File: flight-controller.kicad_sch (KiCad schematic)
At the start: 73 parts, among them J1 USB_C_Receptacle_USB2.0, Q1 AO3400A, SW1 SW_Push, U1 AT32F435RGT7, U2 BMI270, U3 BMP280, U4 W25N01GVZEIG, U5 AT7456E, U6 TPS54302, U7 TPS54302, U8 TLV75733PDBV, U9 USBLC6-2P6, Y1 27MHz

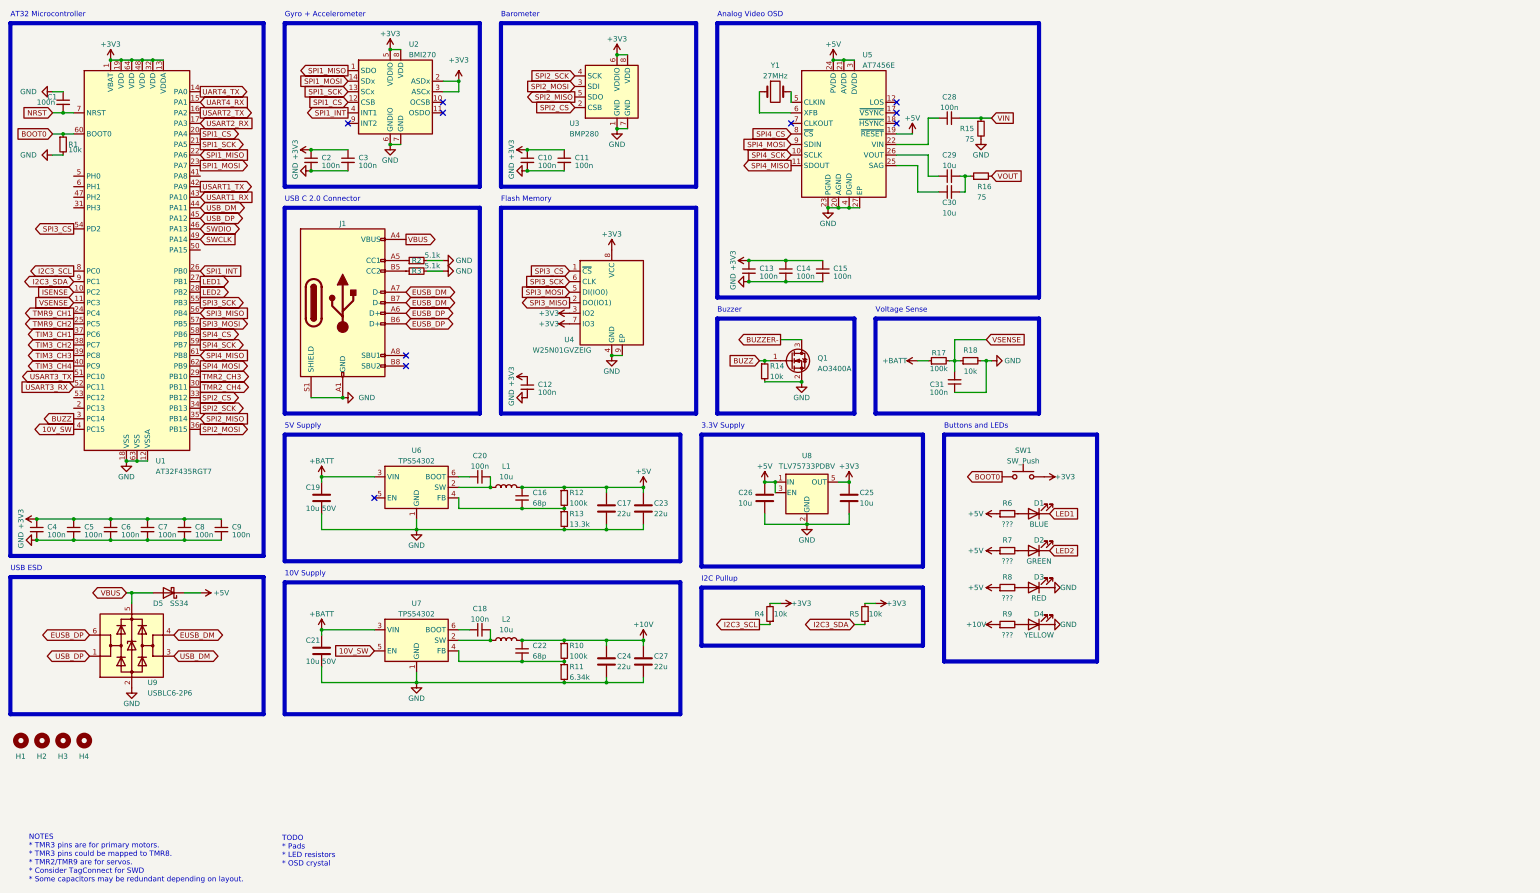
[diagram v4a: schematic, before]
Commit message: Add OSD crystal, minor changes to PCB
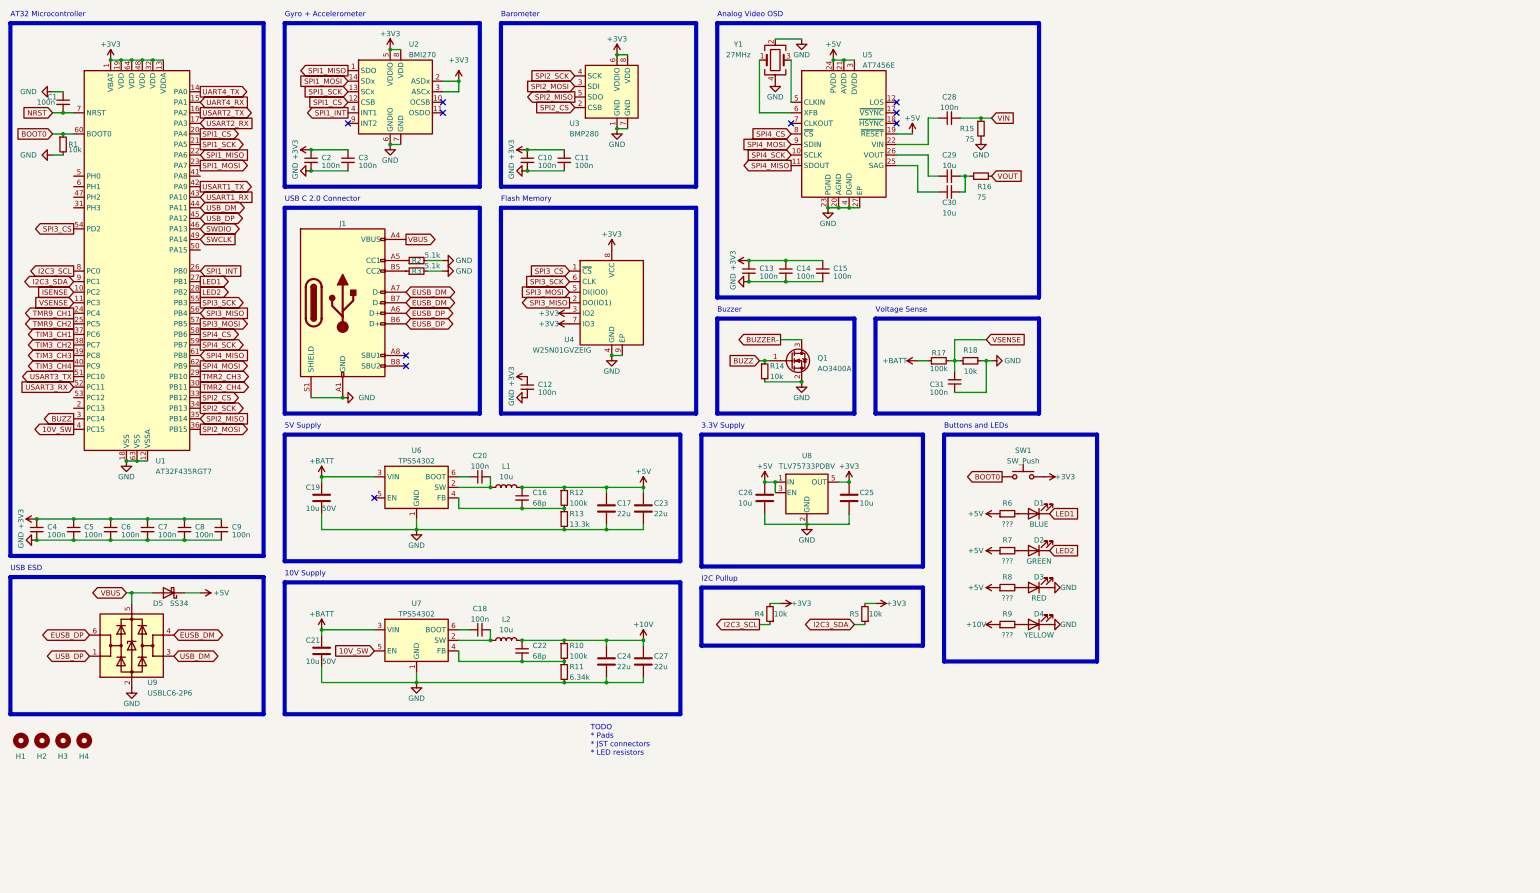
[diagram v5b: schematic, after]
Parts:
- removed Y1: 27MHz, symbol Device:Crystal
- added Y1: 27MHz, Crystal:Crystal_SMD_3225-4Pin_3.2x2.5mm, symbol Device:Crystal_GND24
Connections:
- net GND: now also Y1.2, Y1.4
- net at U5.6 (XFB): now also Y1.1
- net at U5.5 (CLKIN): now also Y1.3
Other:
- note added: "TODO * Pads * JST connectors * LED resistors"
- note removed: "NOTES * TMR3 pins are for primary motors. * TMR3 pins could be mapped to TMR8. * TMR2/TMR9 are for servos. * Consider TagConnect for SWD * Some capacitors may be redundant depending on layout."
- note removed: "TODO * Pads * LED resistors * OSD crystal"
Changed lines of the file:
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@@
     (stroke (width 0) (type default))
   )
+  (wire (pts (xy 199.39 22.86) (xy 205.74 22.86))
+    (stroke (width 0) (type default))
+  )
   (wire (pts (xy 242.57 100.33) (xy 242.57 95.25))
     (stroke (width 0) (type default))
@@
     (stroke (width 0) (type default))
   )
-  (wire (pts (xy 203.2 35.56) (xy 203.2 38.1))
+  (wire (pts (xy 203.2 27.94) (xy 203.2 38.1))
     (stroke (width 0) (type default))
   )
@@
     (stroke (width 0) (type default))
   )
-  (wire (pts (xy 195.58 40.64) (xy 195.58 35.56))
+  (wire (pts (xy 195.58 27.94) (xy 195.58 40.64))
     (stroke (width 0) (type default))
   )
@@
     (effects (font (size 1.27 1.27)) (justify left bottom))
   )
-  (text "TODO\n* Pads\n* LED resistors\n* OSD crystal" (at 80.645 222.25 0)
-    (effects (font (size 1.27 1.27)) (justify left bottom))
-  )
-  (text "NOTES\n* TMR3 pins are for primary motors.\n* TMR3 pins could be mapped to TMR8.\n* TMR2/TMR9 are for servos.\n* Consider TagConnect for SWD\n* Some capacitors may be redundant depending on layout."
-    (at 19.685 226.06 0)
+  (text "TODO\n* Pads\n* JST connectors\n* LED resistors" (at 154.94 195.58 0)
     (effects (font (size 1.27 1.27)) (justify left bottom))
   )
@@
     )
   )
+  (symbol (lib_id "power:GND") (at 205.74 22.86 0) (unit 1)
+    (in_bom yes) (on_board yes) (dnp no)
+    (property "Reference" "#PWR055" (at 205.74 29.21 0)
+      (effects (font (size 1.27 1.27)) hide)
+    )
+    (property "Value" "GND" (at 205.74 26.67 0)
+      (effects (font (size 1.27 1.27)))
+    )
+    (property "Footprint" "" (at 205.74 22.86 0)
+      (effects (font (size 1.27 1.27)) hide)
+    )
+    (property "Datasheet" "" (at 205.74 22.86 0)
+      (effects (font (size 1.27 1.27)) hide)
+    )
+    (pin "1")
+    (instances
+      (project "flight-controller"
+        (path "/1ea4b7d2-6956-4f87-9f61-d89fdcbfe01f"
+          (reference "#PWR055") (unit 1)
+        )
+      )
+    )
+  )
   (symbol (lib_id "Device:C") (at 90.17 170.18 0) (unit 1)
     (in_bom yes) (on_board yes) (dnp no)
@@
     )
   )
-  (symbol (lib_id "Device:Crystal") (at 199.39 35.56 0) (unit 1)
-    (in_bom yes) (on_board yes) (dnp no) (fields_autoplaced)
-    (property "Reference" "Y1" (at 199.39 29.21 0)
-      (effects (font (size 1.27 1.27)))
-    )
-    (property "Value" "27MHz" (at 199.39 31.75 0)
-      (effects (font (size 1.27 1.27)))
-    )
-    (property "Footprint" "" (at 199.39 35.56 0)
-      (effects (font (size 1.27 1.27)) hide)
-    )
-    (property "Datasheet" "~" (at 199.39 35.56 0)
-      (effects (font (size 1.27 1.27)) hide)
-    )
-    (pin "1")
-    (pin "2")
-    (instances
-      (project "flight-controller"
-        (path "/1ea4b7d2-6956-4f87-9f61-d89fdcbfe01f"
-          (reference "Y1") (unit 1)
-        )
-      )
-    )
-  )
   (symbol (lib_id "Device:R_Small") (at 255.27 146.05 90) (unit 1)
     (in_bom yes) (on_board yes) (dnp no)
@@
     )
   )
+  (symbol (lib_id "Device:Crystal_GND24") (at 199.39 27.94 0) (unit 1)
+    (in_bom yes) (on_board yes) (dnp no)
+    (property "Reference" "Y1" (at 190.5 24.13 0)
+      (effects (font (size 1.27 1.27)))
+    )
+    (property "Value" "27MHz" (at 190.5 26.67 0)
+      (effects (font (size 1.27 1.27)))
+    )
+    (property "Footprint" "Crystal:Crystal_SMD_3225-4Pin_3.2x2.5mm" (at 199.39 27.94 0)
+      (effects (font (size 1.27 1.27)) hide)
+    )
+    (property "Datasheet" "~" (at 199.39 27.94 0)
+      (effects (font (size 1.27 1.27)) hide)
+    )
+    (property "LCSC" "C9008" (at 199.39 27.94 0)
+      (effects (font (size 1.27 1.27)) hide)
+    )
+    (pin "1")
+    (pin "2")
+    (pin "3")
+    (pin "4")
+    (instances
+      (project "flight-controller"
+        (path "/1ea4b7d2-6956-4f87-9f61-d89fdcbfe01f"
+          (reference "Y1") (unit 1)
+        )
+      )
+    )
+  )
   (symbol (lib_id "Device:C") (at 90.17 133.35 0) (unit 1)
     (in_bom yes) (on_board yes) (dnp no)
@@
         )
       )
+    )
+  )
+  (symbol (lib_id "power:GND") (at 199.39 33.02 0) (unit 1)
+    (in_bom yes) (on_board yes) (dnp no)
+    (property "Reference" "#PWR054" (at 199.39 39.37 0)
+      (effects (font (size 1.27 1.27)) hide)
+    )
+    (property "Value" "GND" (at 199.39 36.83 0)
+      (effects (font (size 1.27 1.27)))
+    )
+    (property "Footprint" "" (at 199.39 33.02 0)
+      (effects (font (size 1.27 1.27)) hide)
+    )
+    (property "Datasheet" "" (at 199.39 33.02 0)
+      (effects (font (size 1.27 1.27)) hide)
+    )
+    (pin "1")
+    (instances
+      (project "flight-controller"
+        (path "/1ea4b7d2-6956-4f87-9f61-d89fdcbfe01f"
+          (reference "#PWR054") (unit 1)
+        )
+      )

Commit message: Add JST connectors
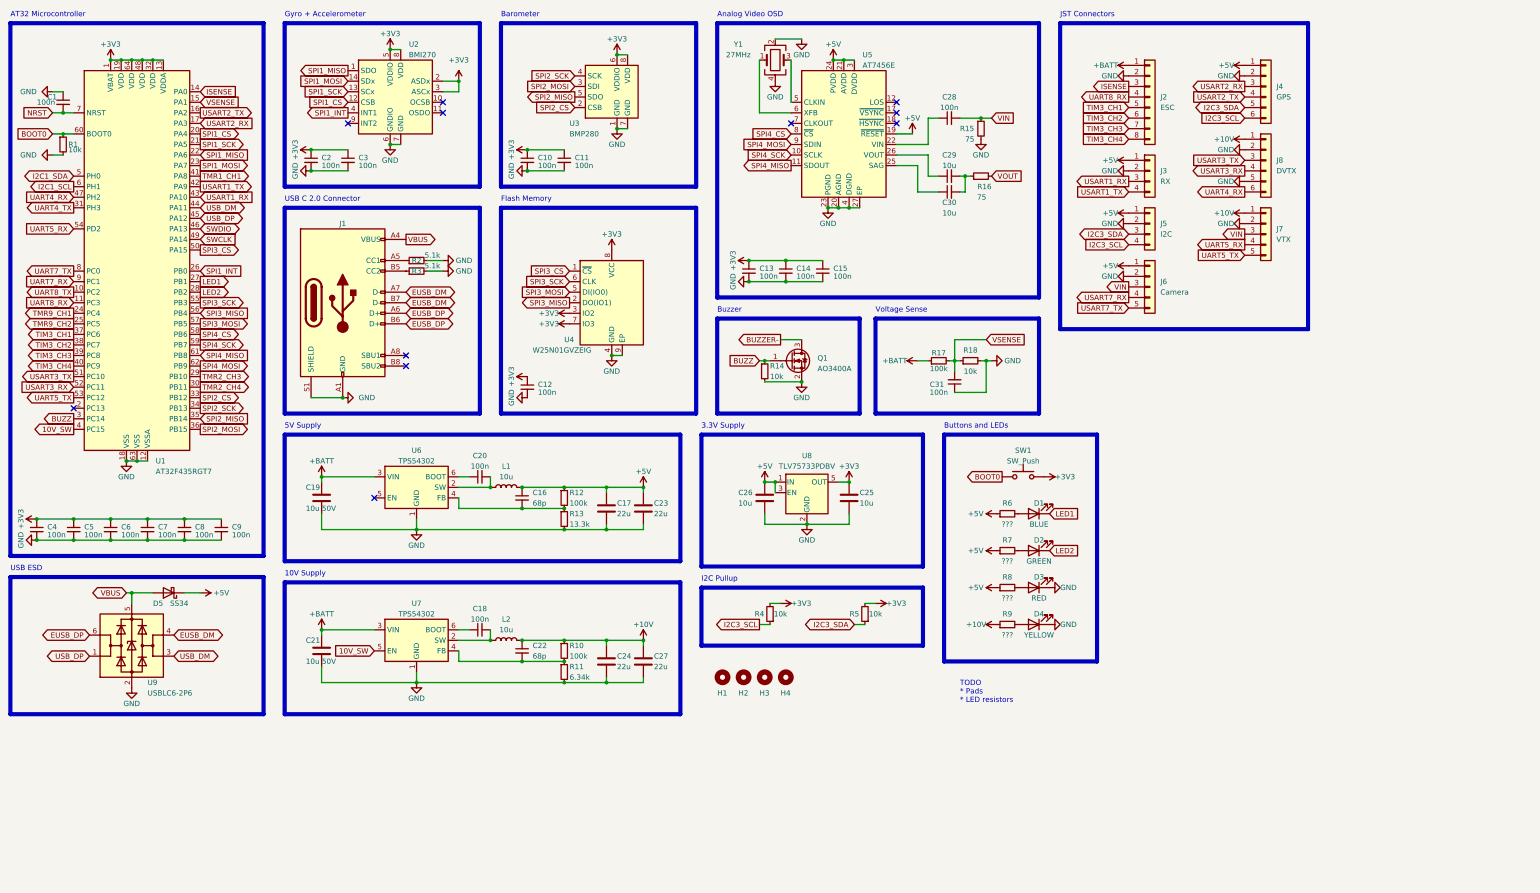
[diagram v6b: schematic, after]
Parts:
- added J2: ESC, Connector_JST:JST_SH_SM08B-SRSS-TB_1x08-1MP_P1.00mm_Horizontal, symbol Connector_Generic:Conn_01x08
- added J3: RX, Connector_JST:JST_SH_SM04B-SRSS-TB_1x04-1MP_P1.00mm_Horizontal, symbol Connector_Generic:Conn_01x04
- added J4: GPS, Connector_JST:JST_SH_SM06B-SRSS-TB_1x06-1MP_P1.00mm_Horizontal, symbol Connector_Generic:Conn_01x06
- added J5: I2C, Connector_JST:JST_SH_SM04B-SRSS-TB_1x04-1MP_P1.00mm_Horizontal, symbol Connector_Generic:Conn_01x04
- added J6: Camera, Connector_JST:JST_SH_SM05B-SRSS-TB_1x05-1MP_P1.00mm_Horizontal, symbol Connector_Generic:Conn_01x05
- added J7: VTX, Connector_JST:JST_SH_SM05B-SRSS-TB_1x05-1MP_P1.00mm_Horizontal, symbol Connector_Generic:Conn_01x05
- added J8: DVTX, Connector_JST:JST_SH_SM06B-SRSS-TB_1x06-1MP_P1.00mm_Horizontal, symbol Connector_Generic:Conn_01x06
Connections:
- net +10V: now also J7.1 (Pin_1), J8.1 (Pin_1)
- net +5V: now also J3.1 (Pin_1), J4.1 (Pin_1), J5.1 (Pin_1), J6.1 (Pin_1)
- net +BATT: now also J2.1 (Pin_1)
- net GND: now also J2.2 (Pin_2), J3.2 (Pin_2), J4.2 (Pin_2), J5.2 (Pin_2), J6.2 (Pin_2), J7.2 (Pin_2), J8.2 (Pin_2), J8.5 (Pin_5)
- net I2C3_SCL: now also J4.6 (Pin_6), J5.4 (Pin_4); no longer U1.8 (PC0)
- net I2C3_SDA: now also J4.5 (Pin_5), J5.3 (Pin_3); no longer U1.9 (PC1)
- net ISENSE: now also U1.14 (PA0), J2.3 (Pin_3); no longer U1.10 (PC2)
- net SPI3_CS: now also U1.50 (PA15); no longer U1.54 (PD2)
- net TIM3_CH1: now also J2.5 (Pin_5)
- net TIM3_CH2: now also J2.6 (Pin_6)
- net TIM3_CH3: now also J2.7 (Pin_7)
- net TIM3_CH4: now also J2.8 (Pin_8)
- net UART4_RX: now also U1.47 (PH2), J8.6 (Pin_6); no longer U1.15 (PA1)
- net UART4_TX: now also U1.31 (PH3); no longer U1.14 (PA0)
- net USART1_RX: now also J3.3 (Pin_3)
- net USART1_TX: now also J3.4 (Pin_4)
- net USART2_RX: now also J4.3 (Pin_3)
- net USART2_TX: now also J4.4 (Pin_4)
- net USART3_RX: now also J8.4 (Pin_4)
- net USART3_TX: now also J8.3 (Pin_3)
- net VIN: now also J6.3 (Pin_3), J7.3 (Pin_3)
- net VSENSE: now also U1.15 (PA1); no longer U1.11 (PC3)
- net TMR1_CH1: now reaches U1.41 (PA8)
- net I2C1_SDA: now reaches U1.5 (PH0)
- net UART5_TX: now reaches U1.53 (PC12)
- net UART5_TX: now also J7.5 (Pin_5)
- net I2C1_SCL: now reaches U1.6 (PH1)
- new net UART5_RX: J7.4 (Pin_4), U1.54 (PD2)
- new net UART7_RX: U1.9 (PC1)
- new net UART7_TX: U1.8 (PC0)
- new net UART8_RX: J2.4 (Pin_4), U1.11 (PC3)
- new net UART8_TX: U1.10 (PC2)
- new net USART7_RX: J6.4 (Pin_4)
- new net USART7_TX: J6.5 (Pin_5)
- no-connect marks 10 -> 11
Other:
- note added: "JST Connectors"
- note added: "TODO * Pads * LED resistors"
- note removed: "TODO * Pads * JST connectors * LED resistors"
- moved on the sheet: H1, H2, H3, H4

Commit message: Add AT32 HSE crystal and choose LED resistors
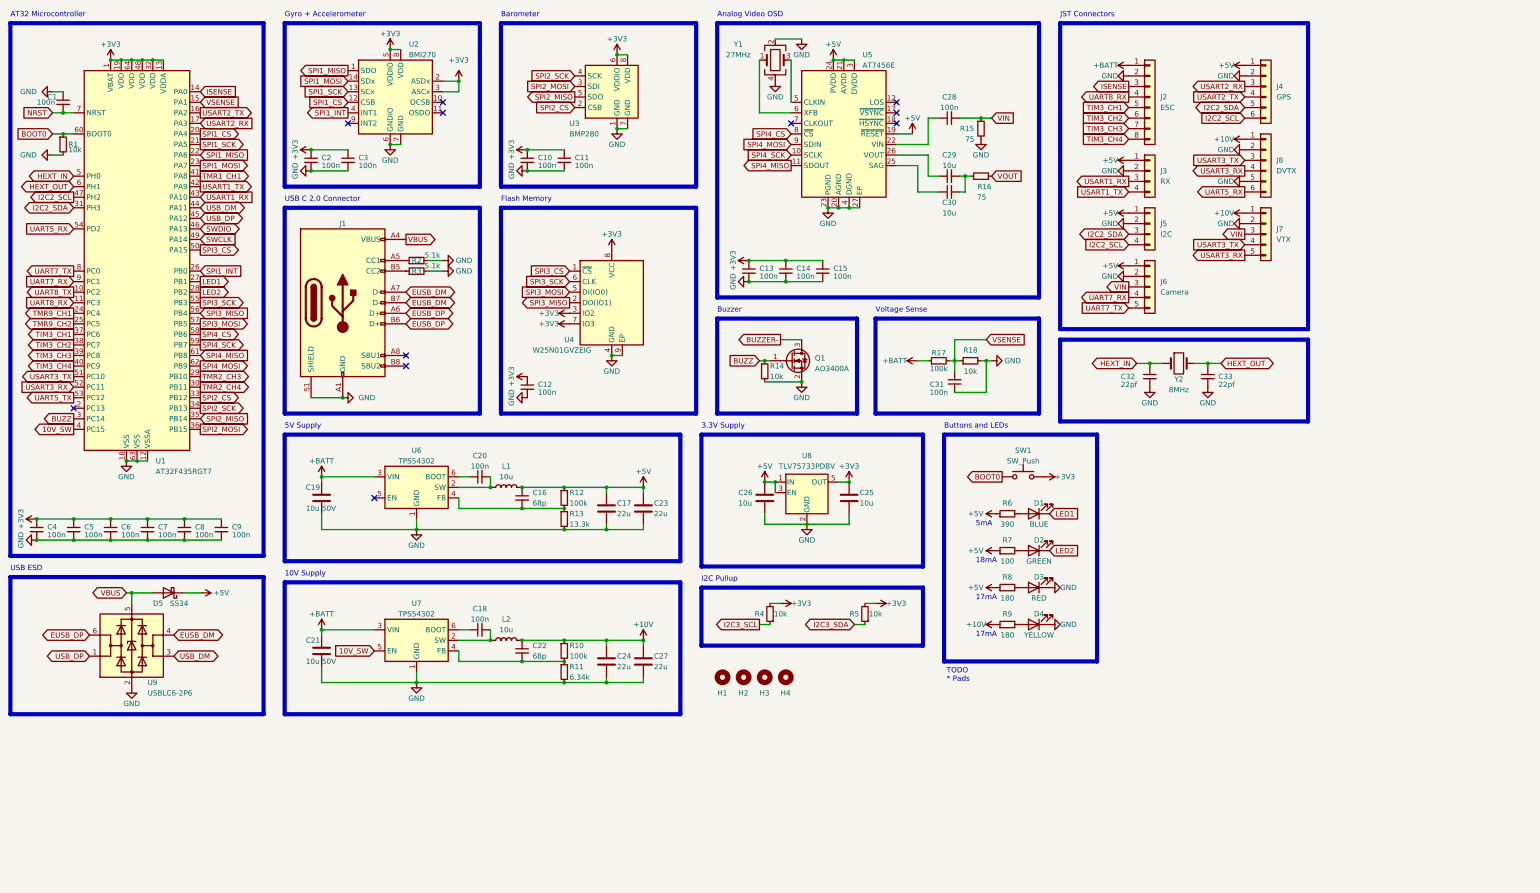
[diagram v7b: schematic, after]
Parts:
- added C32, C33: 22pf, Capacitor_SMD:C_0402_1005Metric, symbol Device:C_Small
- added Y2: 8MHz, Crystal:Crystal_SMD_5032-2Pin_5.0x3.2mm, symbol Device:Crystal
- R6: value ??? -> 390; footprint (none) -> Resistor_SMD:R_0603_1608Metric
- R7: value ??? -> 100; footprint (none) -> Resistor_SMD:R_0603_1608Metric; LCSC (none) -> C22775
- R8, R9: value ??? -> 180; footprint (none) -> Resistor_SMD:R_0603_1608Metric; LCSC (none) -> C22828
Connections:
- net USART7_RX is gone; now on net UART7_RX: J6.4 (Pin_4)
- net USART7_TX is gone; now on net UART7_TX: J6.5 (Pin_5)
- net GND: now also C32.2, C33.2
- net I2C3_SCL: no longer J4.6 (Pin_6), J5.4 (Pin_4)
- net I2C3_SDA: no longer J4.5 (Pin_5), J5.3 (Pin_3)
- net UART5_RX: now also J8.6 (Pin_6); no longer J7.4 (Pin_4)
- net UART5_TX: no longer J7.5 (Pin_5)
- net USART3_RX: now also J7.5 (Pin_5)
- net USART3_TX: now also J7.4 (Pin_4)
- net I2C1_SCL renamed HEXT_OUT
- net HEXT_OUT: now also C33.1, Y2.2
- net I2C1_SDA renamed HEXT_IN
- net HEXT_IN: now also C32.1, Y2.1
- net UART4_RX renamed I2C2_SCL
- net I2C2_SCL: now also J4.6 (Pin_6), J5.4 (Pin_4); no longer J8.6 (Pin_6)
- net UART4_TX renamed I2C2_SDA
- net I2C2_SDA: now also J4.5 (Pin_5), J5.3 (Pin_3)
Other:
- note added: "17mA"
- note added: "18mA"
- note added: "5mA"
- note added: "TODO * Pads"
- note removed: "TODO * Pads * LED resistors"
